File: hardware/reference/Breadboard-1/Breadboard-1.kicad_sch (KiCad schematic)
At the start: 57 parts, among them J1 Left, J2 Right, J3 ICSP, Q31 HSM0903, Q32 HSM0903, Q41 FDG1024NZ, Q42 FDG1024NZ, Q43 FDG1024NZ, U11 AMS1117-5.0, U21 PIC18F25K50-xML

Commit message: Lots of cleanup, finalizing the specifications for Breadboard-1.
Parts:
- C11, C12: Specification (none) -> 0805 50V 10uF X5R 10%
- C21, C22, C23, C31: Specification (none) -> 0402 50V 100nF X7R 10%
- D11, D12, D13, D14, D31, D32, D33, D34: Specification (none) -> SOD-523, 50V, 1A Schottky barrier rectifier diode
- D41, D42, D51, D52, D53, D54, D55, D56: Specification (none) -> 0805, Bright White, 25ma, Vf 2.9v
- J1, J2: Specification (none) -> 6 position 2.54mm pin header
- J3: Specification (none) -> 5 position 2.54mm pin header
- Q31, Q32: Specification (none) -> SOT-8, Vdss 100V, Id 3A
- Q41, Q42, Q43: value FDG1024NZ -> 2N7002; Specification (none) -> SOT-23-6, 2xNPN Vdss 60V Id 300ma
- R21, R36, R51, R52, R53, R54, R55, R56, R57: Specification (none) -> 0402 1.33K Ω 1% 1/8W
- R22, R35: Specification (none) -> 0402 6.65K Ω 1% 1/8W
- R23: Specification (none) -> 0402 10K Ω 1% 1/8W
- R31, R32, R33, R42, R43, R44, R46, R47, R48: Specification (none) -> 0402 220 Ω 1% 1/8W
- R34: value 200 -> 220; Specification (none) -> 0402 220 Ω 1% 1/8W
- R41, R45: Specification (none) -> 0402 470 Ω 1% 1/8W
- U11: Specification (none) -> 5V Linear Regulator
- U21: Specification (none) -> PIC18F Series Micro-Processor
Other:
- note added: "Rail power is fed into a bridge rectifier to generate 6-30V DC which is referenced as Vdrive. An AMS1117 5V Linear Regulator generates power for the micro-controller."
- note removed: "Rail power is fed into a bridge rectifier to generate ~+12V DC. An AMS1117 5V Linear Regulator generates power for the uC."

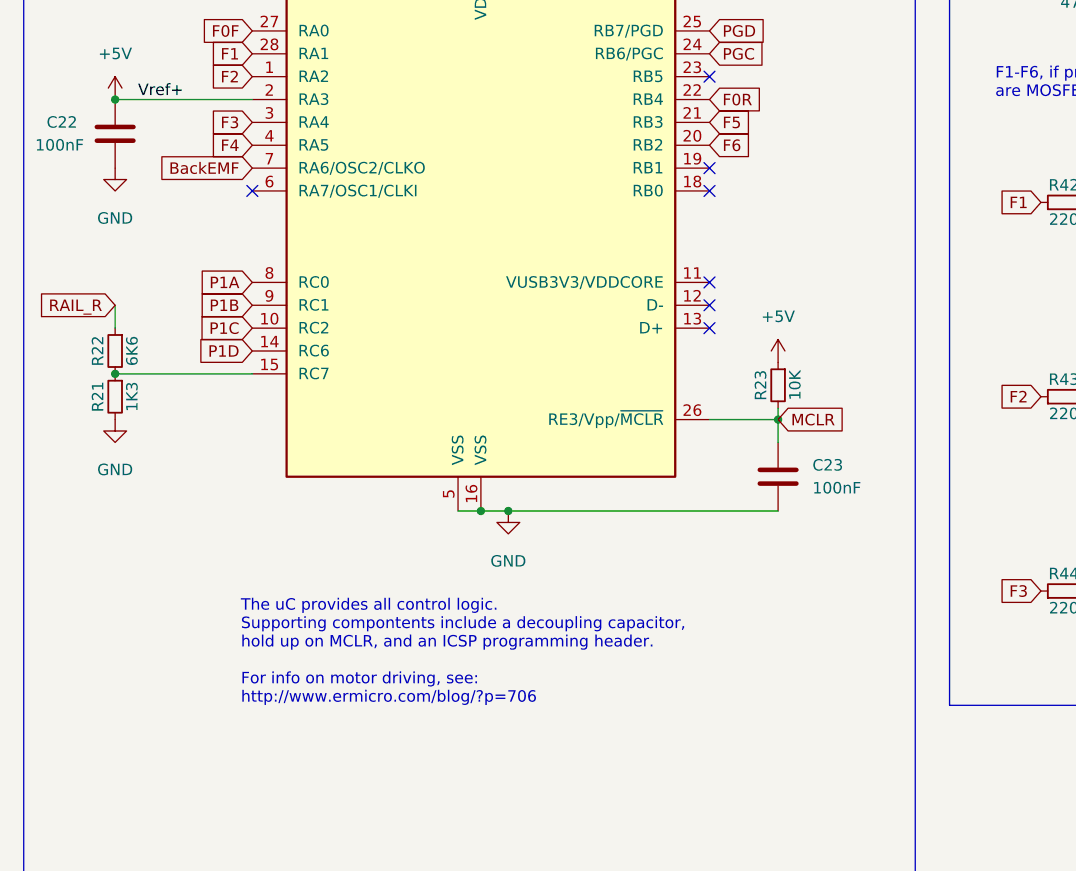
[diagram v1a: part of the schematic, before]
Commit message: Added V3V3USB capacitor and USB Micro-B port for debugging.
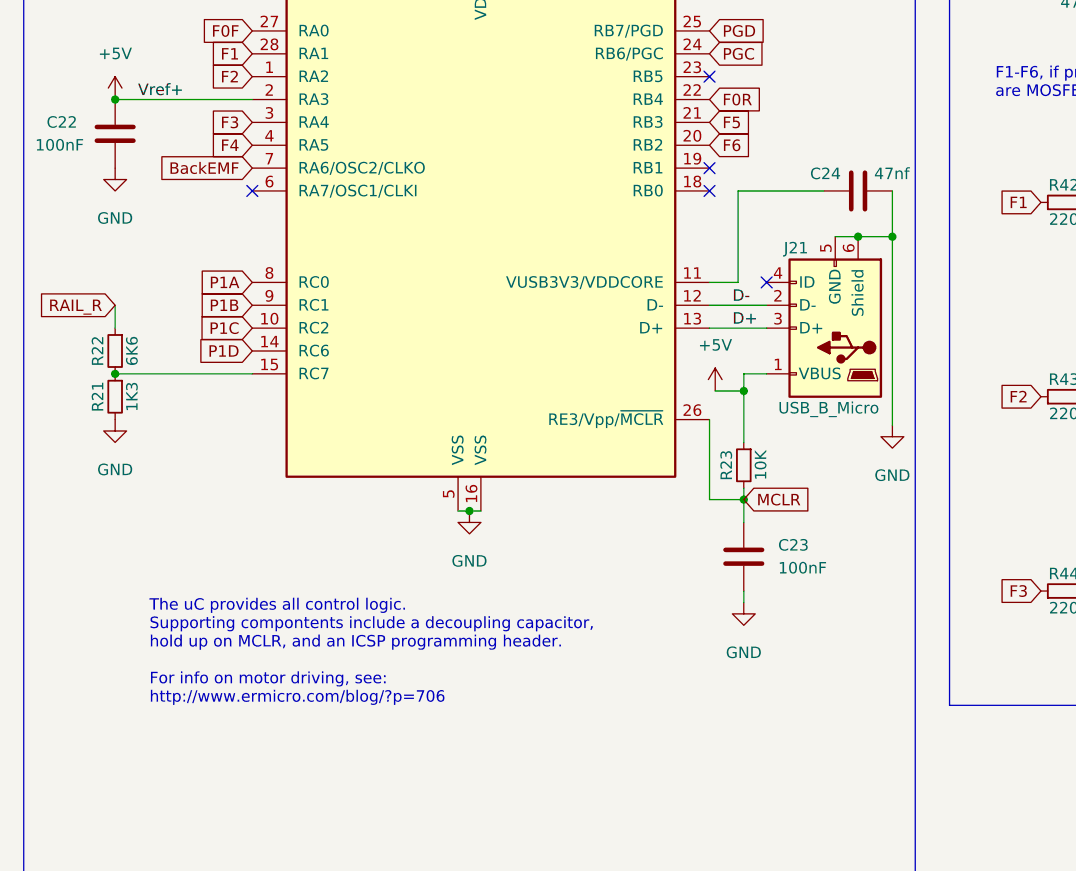
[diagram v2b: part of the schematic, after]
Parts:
- added C24: 47nf, Capacitor_SMD:C_0402_1005Metric, symbol Device:C
- added J21: USB_B_Micro, Connector_USB:USB_Micro-B_Wuerth_629105150521, symbol Connector:USB_B_Micro
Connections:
- net +5V: now also J21.1 (VBUS)
- net GND: now also C24.1, J21.5 (GND), J21.6 (Shield)
- net at U21.11 (VUSB3V3/VDDCORE): now also C24.2
- net D-: now reaches U21.12 (D-)
- net D-: now also J21.2 (D-)
- net D+: now reaches U21.13 (D+)
- net D+: now also J21.3 (D+)
- no-connect marks 7 -> 5
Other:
- moved on the sheet: C23, R23

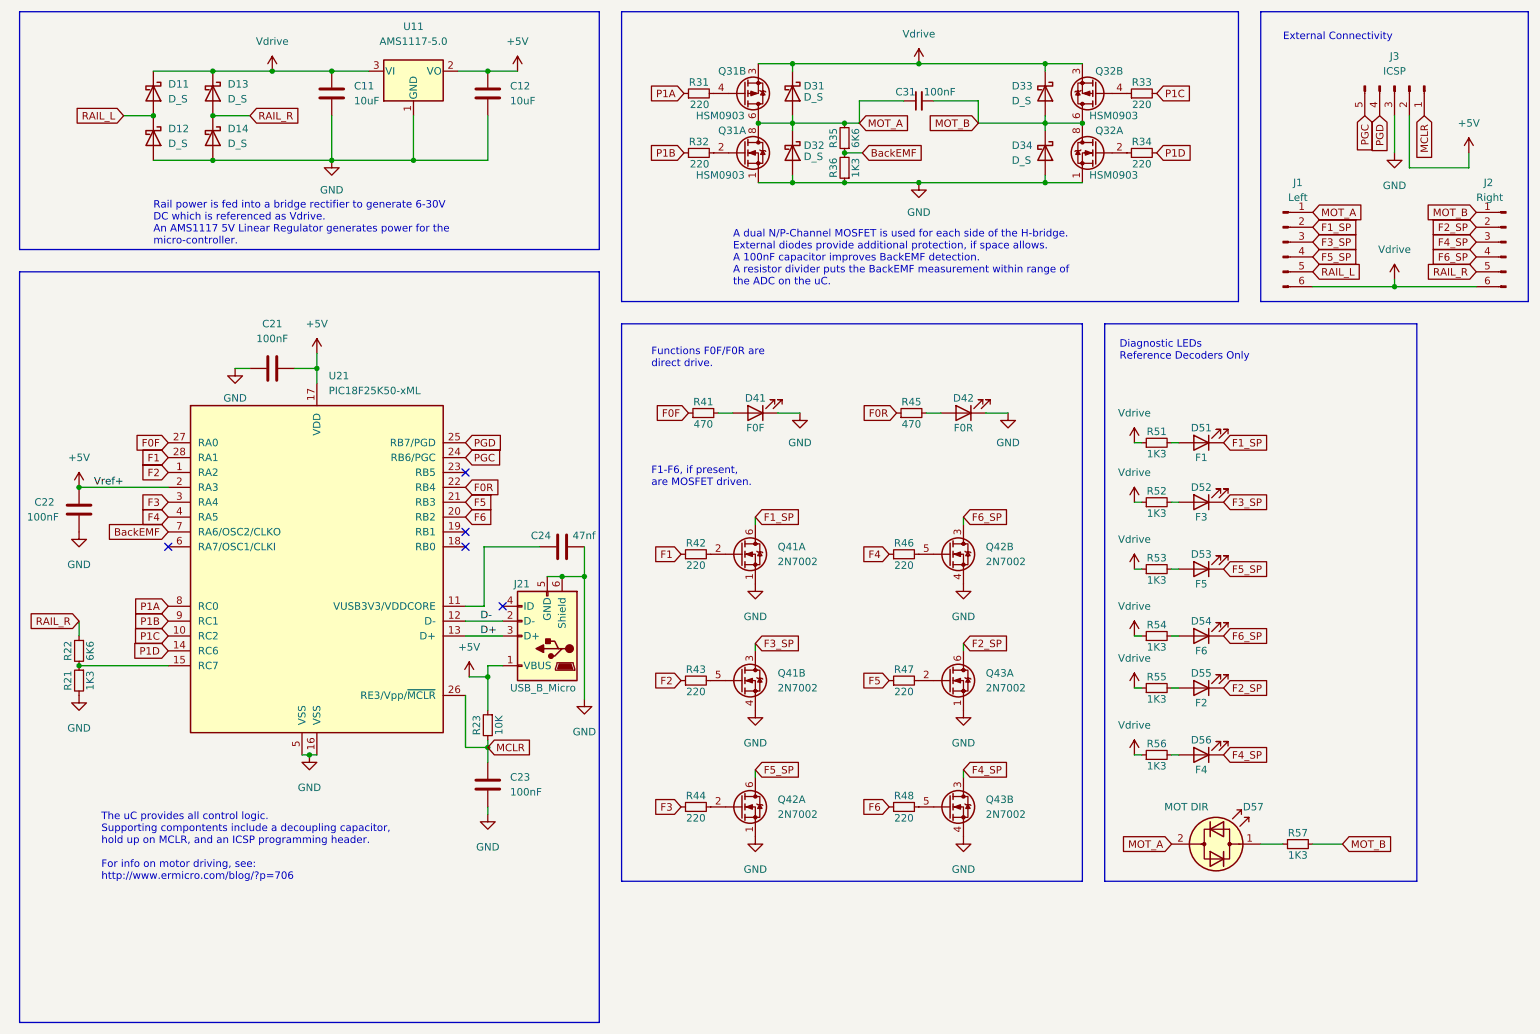
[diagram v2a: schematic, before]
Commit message: Move USB to the External Connectivity section.
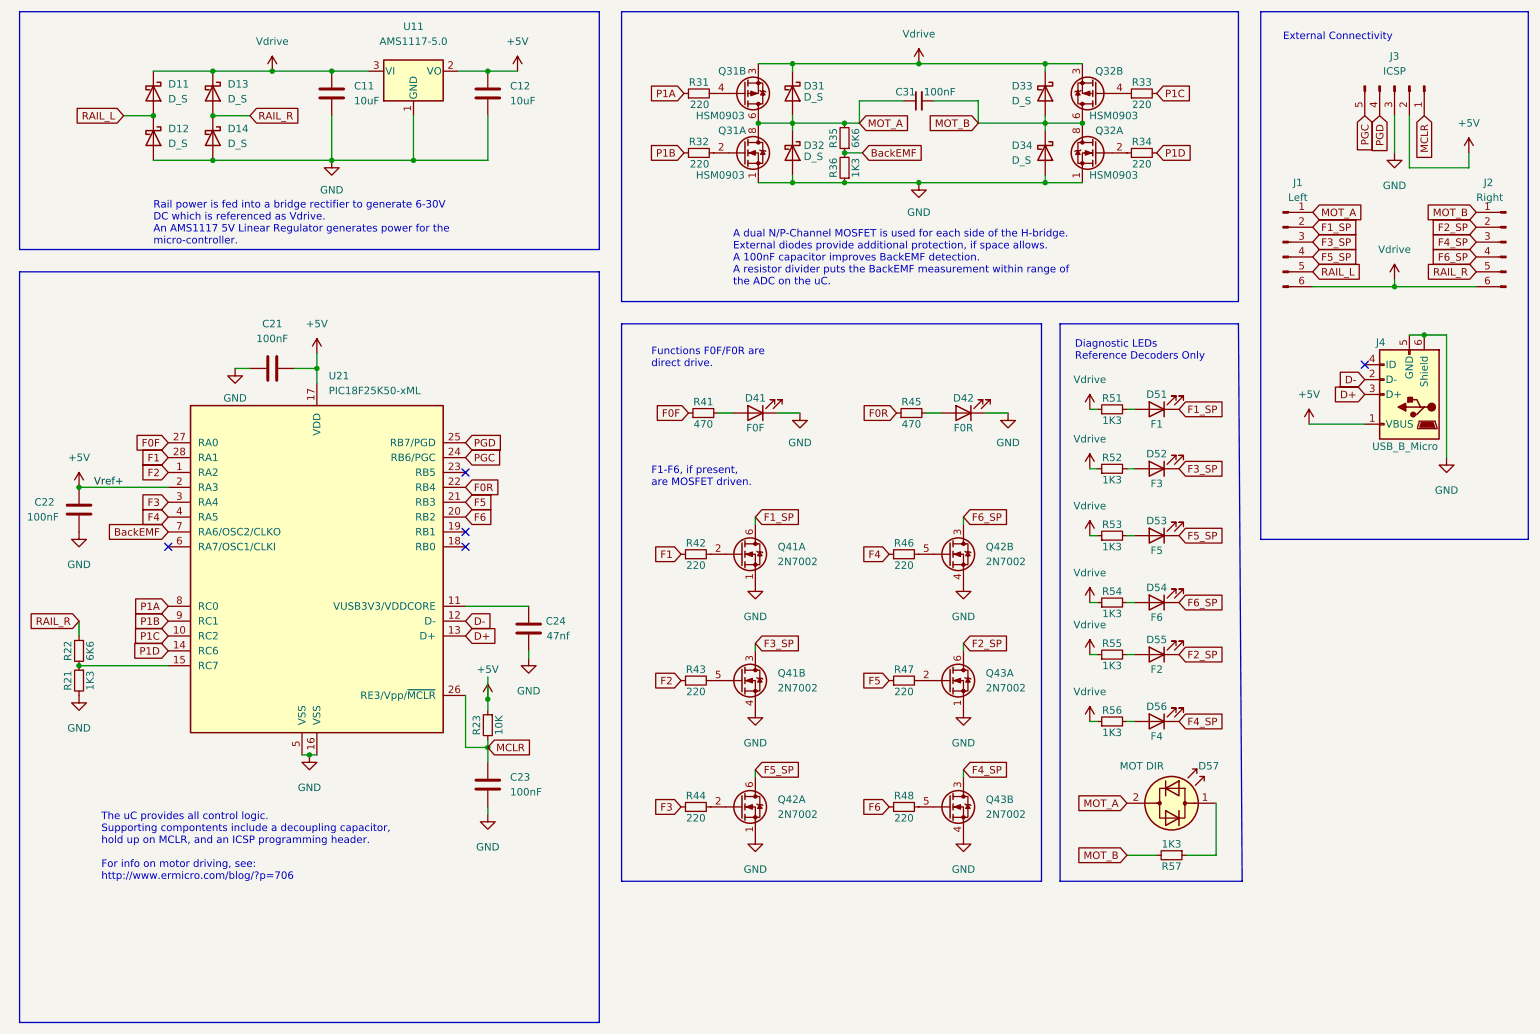
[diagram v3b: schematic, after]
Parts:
- renumbered J21 to J4
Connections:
- net GND: now also C24.2; no longer C24.1
- net at U21.11 (VUSB3V3/VDDCORE): now also C24.1; no longer C24.2
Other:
- moved on the sheet: C24, D51, D52, D53, D54, D55, D56, D57, J4, R51, R52, R53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

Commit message: Update notes to be more clear about circuit design.
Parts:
- C24: Specification 0402 50V 100nF X7R 10% -> 0402 50V 47nF X7R 10%
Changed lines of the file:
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@@
       (effects (font (size 1.27 1.27)) hide)
     )
-    (property "Specification" "0402 50V 100nF X7R 10%" (id 4) (at 102.235 120.65 0)
+    (property "Specification" "0402 50V 47nF X7R 10%" (id 4) (at 102.235 120.65 0)
       (effects (font (size 1.27 1.27)) hide)
     )

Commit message: Moved to SOD-123 diodes for cheaper, better rating parts.
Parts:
- D11, D12, D13, D14: footprint Diode_SMD:D_SOD-523 -> Diode_SMD:D_SOD-128
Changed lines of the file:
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@@
       (effects (font (size 1.27 1.27)) (justify left))
     )
-    (property "Footprint" "Diode_SMD:D_SOD-523" (id 2) (at 38.1 36.83 0)
+    (property "Footprint" "Diode_SMD:D_SOD-128" (id 2) (at 38.1 36.83 0)
       (effects (font (size 1.27 1.27)) hide)
     )
@@
       (effects (font (size 1.27 1.27)) (justify left))
     )
-    (property "Footprint" "Diode_SMD:D_SOD-523" (id 2) (at 48.26 36.83 0)
+    (property "Footprint" "Diode_SMD:D_SOD-128" (id 2) (at 48.26 36.83 0)
       (effects (font (size 1.27 1.27)) hide)
     )
@@
       (effects (font (size 1.27 1.27)) (justify left))
     )
-    (property "Footprint" "Diode_SMD:D_SOD-523" (id 2) (at 38.1 29.21 0)
+    (property "Footprint" "Diode_SMD:D_SOD-128" (id 2) (at 38.1 29.21 0)
       (effects (font (size 1.27 1.27)) hide)
     )
@@
       (effects (font (size 1.27 1.27)) (justify left))
     )
-    (property "Footprint" "Diode_SMD:D_SOD-523" (id 2) (at 48.26 29.21 0)
+    (property "Footprint" "Diode_SMD:D_SOD-128" (id 2) (at 48.26 29.21 0)
       (effects (font (size 1.27 1.27)) hide)
     )
@@
     )
     (path "/8804ac3b-c636-4dd9-97bf-f0c4cc720a24"
-      (reference "D11") (unit 1) (value "D_S") (footprint "Diode_SMD:D_SOD-523")
+      (reference "D11") (unit 1) (value "D_S") (footprint "Diode_SMD:D_SOD-128")
     )
     (path "/1834d5fc-5be1-4603-87bc-02d57ced0a00"
-      (reference "D12") (unit 1) (value "D_S") (footprint "Diode_SMD:D_SOD-523")
+      (reference "D12") (unit 1) (value "D_S") (footprint "Diode_SMD:D_SOD-128")
     )
     (path "/fddf5303-69f1-4667-b95d-772b9bae08fb"
-      (reference "D13") (unit 1) (value "D_S") (footprint "Diode_SMD:D_SOD-523")
+      (reference "D13") (unit 1) (value "D_S") (footprint "Diode_SMD:D_SOD-128")
     )
     (path "/7ddb92cb-6fe3-4842-b451-049e9389ed25"
-      (reference "D14") (unit 1) (value "D_S") (footprint "Diode_SMD:D_SOD-523")
+      (reference "D14") (unit 1) (value "D_S") (footprint "Diode_SMD:D_SOD-128")
     )
     (path "/7e63b9a3-985a-4a18-9207-41e901119525"
